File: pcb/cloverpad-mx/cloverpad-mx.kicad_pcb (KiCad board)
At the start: 2 copper layers, 70 x 70 mm, 42 parts, among them J1 USB_C_Receptacle_USB2.0, SW1 SW_Push, SW2 SW_Push, U1 SRV05-4, U2 XC6206P332MR, U8 RP2040, U9 W25Q16JVSSIQ, Y1 12MHz

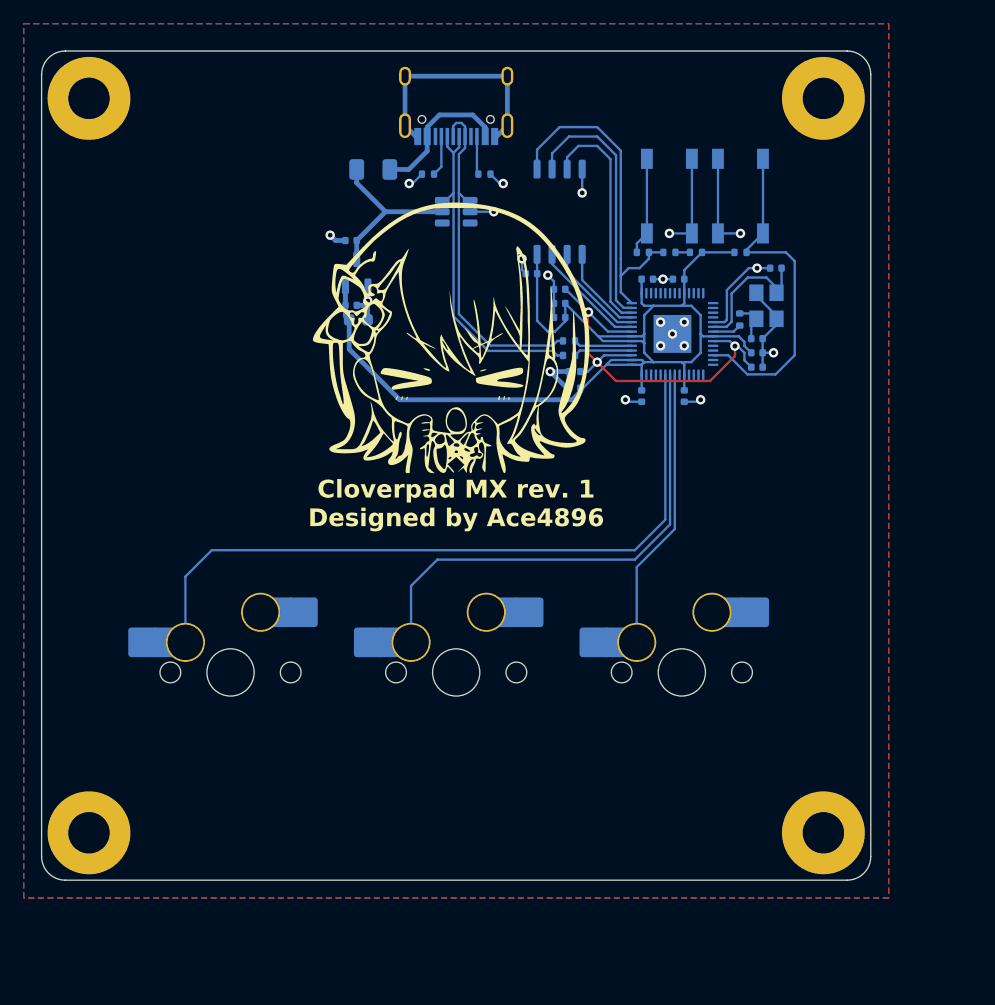
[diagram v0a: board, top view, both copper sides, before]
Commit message: fix: port pcb shape changes to cloverpad mx
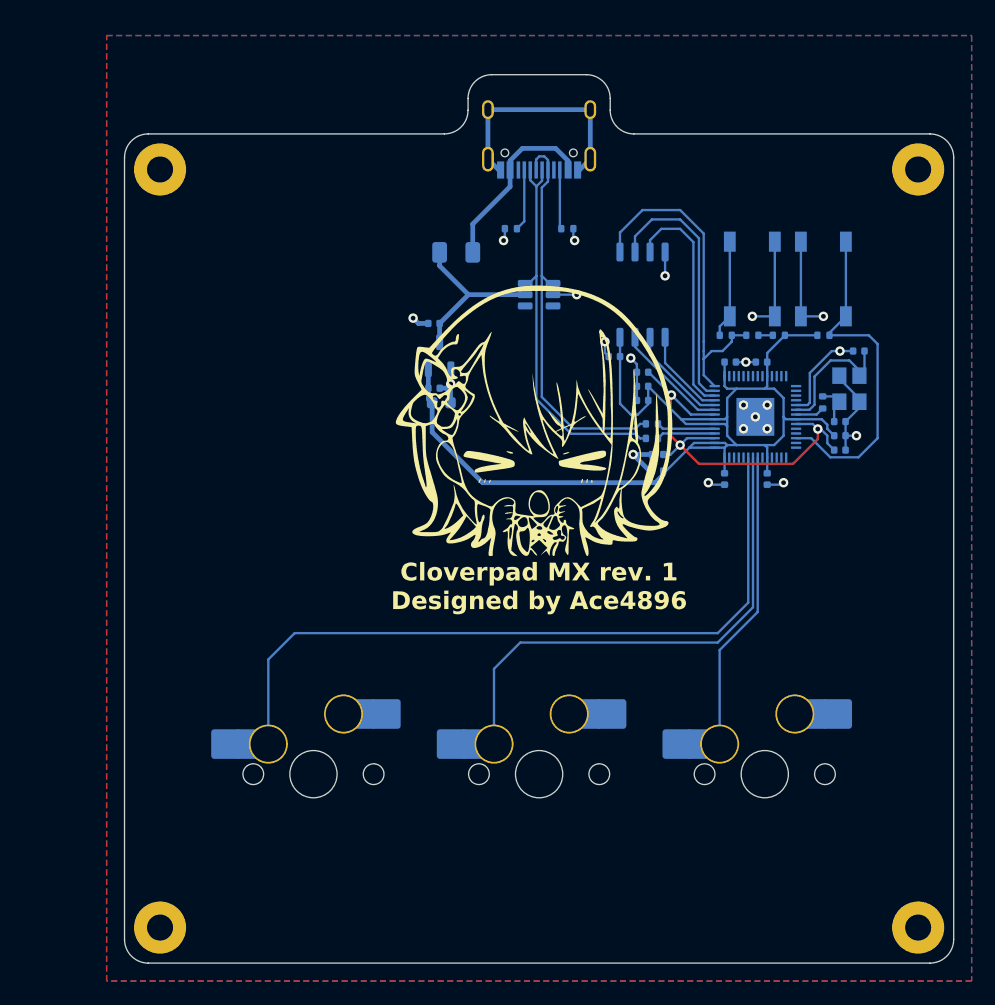
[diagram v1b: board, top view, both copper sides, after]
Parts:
- H1, H2, H3, H4: footprint MountingHole:MountingHole_3.5mm_Pad -> MountingHole:MountingHole_2.2mm_M2_Pad
- moved H4 11.3 mm to (89.8, 89.8)
- moved MX1 11.1 mm to (76.8, 76.8)
- moved MX2 11.1 mm to (57.8, 76.8)
- moved MX3 11.1 mm to (38.8, 76.8)
- moved H2 10.0 mm to (89.8, 25.8)
- moved H3 10.0 mm to (25.8, 89.8)
- moved C12 9.90 mm to (67.8, 49.9)
- moved C16 9.90 mm to (67.8, 51.3)
- moved C13 9.90 mm to (66.5, 42.9)
- moved C14 9.90 mm to (83.2, 49.5)
- moved C15 9.90 mm to (49.5, 45.5)
- moved C17 9.90 mm to (66.5, 45.3)
- moved C18 9.90 mm to (66.5, 44.1)
- moved C19 9.90 mm to (73.5, 51.9)
- moved C20 9.90 mm to (77.1, 51.9)
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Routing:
- net D+: track 29.4 -> 33.6 mm
- net D-: track 28.8 -> 33.0 mm
- net VBUS: track 12.3 -> 15.6 mm
- net Net-(J1-CC2): track 3.22 -> 5.01 mm
- net Net-(J1-CC1): track 3.43 -> 5.21 mm
- net K3: track 60.3 -> 61.9 mm
- net K2: track 41.4 -> 43.0 mm
- net K1: track 23.9 -> 25.5 mm
- net GND: track 80.1 -> 79.4 mm
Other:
- board size 70 x 70 mm -> 70 x 75 mm

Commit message: fix: swap positions of MX1 and MX3 on cloverpad mx
makes more sense as when viewed from the front, MX1 is the leftmost switch.
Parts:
- moved MX1 38.1 mm to (38.7, 76.9)
- moved MX3 38.1 mm to (76.9, 76.8)
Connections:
- U8 pad 35: K1 -> K3
- U8 pad 37: K3 -> K1
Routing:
- net K3: track 61.9 -> 25.5 mm
- net K1: track 25.5 -> 61.9 mm
